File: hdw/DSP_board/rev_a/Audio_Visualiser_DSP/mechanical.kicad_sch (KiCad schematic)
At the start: 0 parts

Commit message: more schematic progress
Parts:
- added H? (x4): MountingHole, MountingHole:MountingHole_3mm, symbol Mechanical:MountingHole
- added MK? (x4): Screw, symbol Custom Library:Screw
- added MK? (x4): Standoff, symbol Custom Library:Standoff

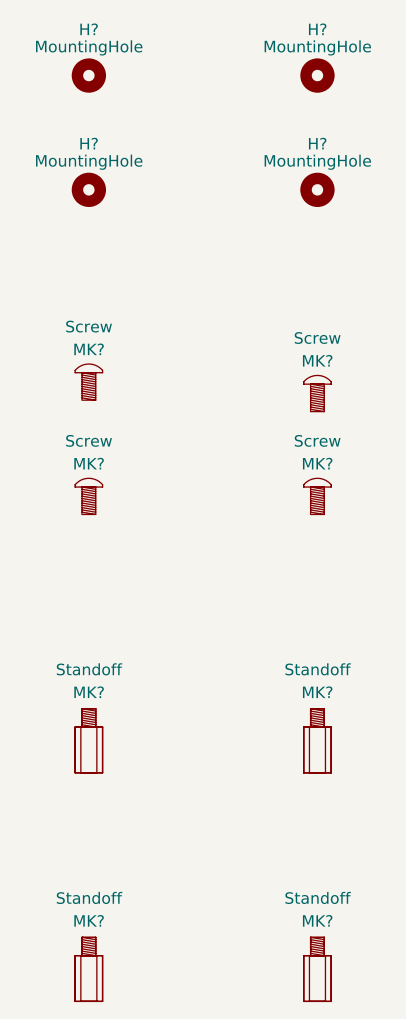
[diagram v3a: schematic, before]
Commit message: Added some spice models
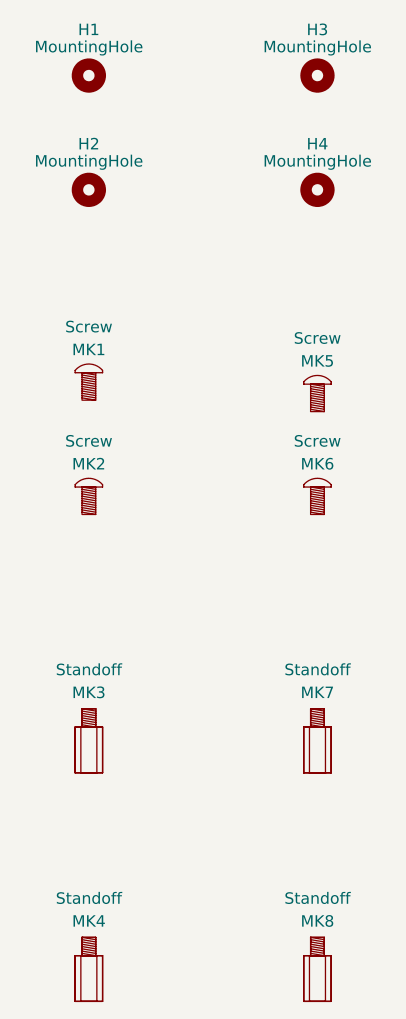
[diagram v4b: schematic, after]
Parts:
- gave numbers to parts that had none: 12
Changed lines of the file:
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@@
 		(in_pos_files yes)
 		(dnp no)
-		(property "Reference" "MK?"
+		(property "Reference" "MK6"
 			(at 139.7 99.06 0)
 			(show_name no)
@@
 			(project "Audio_Visualiser_DSP"
 				(path "/97a4dfb8-0e16-46f1-9709-8d2007dd0cd3/0b5ba344-fa98-45fc-87ea-1c2bd832dac8"
-					(reference "MK?")
+					(reference "MK6")
 					(unit 1)
 				)
@@
 		(in_pos_files yes)
 		(dnp no)
-		(property "Reference" "H?"
+		(property "Reference" "H3"
 			(at 139.7 50.8 0)
 			(show_name no)
@@
 			(project "Audio_Visualiser_DSP"
 				(path "/97a4dfb8-0e16-46f1-9709-8d2007dd0cd3/0b5ba344-fa98-45fc-87ea-1c2bd832dac8"
-					(reference "H?")
+					(reference "H3")
 					(unit 1)
 				)
@@
 		(in_pos_files yes)
 		(dnp no)
-		(property "Reference" "MK?"
+		(property "Reference" "MK7"
 			(at 139.7 124.46 0)
 			(show_name no)
@@
 			(project "Audio_Visualiser_DSP"
 				(path "/97a4dfb8-0e16-46f1-9709-8d2007dd0cd3/0b5ba344-fa98-45fc-87ea-1c2bd832dac8"
-					(reference "MK?")
+					(reference "MK7")
 					(unit 1)
 				)
@@
 		(in_pos_files yes)
 		(dnp no)
-		(property "Reference" "MK?"
+		(property "Reference" "MK3"
 			(at 114.3 124.46 0)
 			(show_name no)
@@
 			(project "Audio_Visualiser_DSP"
 				(path "/97a4dfb8-0e16-46f1-9709-8d2007dd0cd3/0b5ba344-fa98-45fc-87ea-1c2bd832dac8"
-					(reference "MK?")
+					(reference "MK3")
 					(unit 1)
 				)
@@
 		(in_pos_files yes)
 		(dnp no)
-		(property "Reference" "MK?"
+		(property "Reference" "MK1"
 			(at 114.3 86.36 0)
 			(show_name no)
@@
 			(project "Audio_Visualiser_DSP"
 				(path "/97a4dfb8-0e16-46f1-9709-8d2007dd0cd3/0b5ba344-fa98-45fc-87ea-1c2bd832dac8"
-					(reference "MK?")
+					(reference "MK1")
 					(unit 1)
 				)
@@
 		(in_pos_files yes)
 		(dnp no)
-		(property "Reference" "MK?"
+		(property "Reference" "MK2"
 			(at 114.3 99.06 0)
 			(show_name no)
@@
 			(project "Audio_Visualiser_DSP"
 				(path "/97a4dfb8-0e16-46f1-9709-8d2007dd0cd3/0b5ba344-fa98-45fc-87ea-1c2bd832dac8"
-					(reference "MK?")
+					(reference "MK2")
 					(unit 1)
 				)
@@
 		(in_pos_files yes)
 		(dnp no)
-		(property "Reference" "MK?"
+		(property "Reference" "MK8"
 			(at 139.7 149.86 0)
 			(show_name no)
@@
 			(project "Audio_Visualiser_DSP"
 				(path "/97a4dfb8-0e16-46f1-9709-8d2007dd0cd3/0b5ba344-fa98-45fc-87ea-1c2bd832dac8"
-					(reference "MK?")
+					(reference "MK8")
 					(unit 1)
 				)
@@
 		(in_pos_files yes)
 		(dnp no)
-		(property "Reference" "H?"
+		(property "Reference" "H2"
 			(at 114.3 63.5 0)
 			(show_name no)
@@
 			(project "Audio_Visualiser_DSP"
 				(path "/97a4dfb8-0e16-46f1-9709-8d2007dd0cd3/0b5ba344-fa98-45fc-87ea-1c2bd832dac8"
-					(reference "H?")
+					(reference "H2")
 					(unit 1)
 				)
@@
 		(in_pos_files yes)
 		(dnp no)
-		(property "Reference" "MK?"
+		(property "Reference" "MK5"
 			(at 139.7 87.63 0)
 			(show_name no)
@@
 			(project "Audio_Visualiser_DSP"
 				(path "/97a4dfb8-0e16-46f1-9709-8d2007dd0cd3/0b5ba344-fa98-45fc-87ea-1c2bd832dac8"
-					(reference "MK?")
+					(reference "MK5")
 					(unit 1)
 				)
@@
 		(in_pos_files yes)
 		(dnp no)
-		(property "Reference" "H?"
+		(property "Reference" "H4"
 			(at 139.7 63.5 0)
 			(show_name no)
@@
 			(project "Audio_Visualiser_DSP"
 				(path "/97a4dfb8-0e16-46f1-9709-8d2007dd0cd3/0b5ba344-fa98-45fc-87ea-1c2bd832dac8"
-					(reference "H?")
+					(reference "H4")
 					(unit 1)
 				)
@@
 		(in_pos_files yes)
 		(dnp no)
-		(property "Reference" "H?"
+		(property "Reference" "H1"
 			(at 114.3 50.8 0)
 			(show_name no)
@@
 			(project "Audio_Visualiser_DSP"
 				(path "/97a4dfb8-0e16-46f1-9709-8d2007dd0cd3/0b5ba344-fa98-45fc-87ea-1c2bd832dac8"
-					(reference "H?")
+					(reference "H1")
 					(unit 1)
 				)
@@
 		(in_pos_files yes)
 		(dnp no)
-		(property "Reference" "MK?"
+		(property "Reference" "MK4"
 			(at 114.3 149.86 0)
 			(show_name no)
@@
 			(project "Audio_Visualiser_DSP"
 				(path "/97a4dfb8-0e16-46f1-9709-8d2007dd0cd3/0b5ba344-fa98-45fc-87ea-1c2bd832dac8"
-					(reference "MK?")
-					(unit 1)
-				)
+					(reference "MK4")
+					(unit 1)
+				)

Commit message: Annotated schematic
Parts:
- renumbered H1 to H2001, H2 to H2002, H3 to H2003, H4 to H2004, MK1 to MK2001, MK2 to MK2002, MK3 to MK2003, MK4 to MK2004, MK5 to MK2005, MK6 to MK2006, MK7 to MK2007, MK8 to MK2008
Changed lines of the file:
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@@
 		(in_pos_files yes)
 		(dnp no)
-		(property "Reference" "MK6"
+		(property "Reference" "MK2006"
 			(at 139.7 99.06 0)
 			(show_name no)
@@
 			(project "Audio_Visualiser_DSP"
 				(path "/97a4dfb8-0e16-46f1-9709-8d2007dd0cd3/0b5ba344-fa98-45fc-87ea-1c2bd832dac8"
-					(reference "MK6")
+					(reference "MK2006")
 					(unit 1)
 				)
@@
 		(in_pos_files yes)
 		(dnp no)
-		(property "Reference" "H3"
+		(property "Reference" "H2003"
 			(at 139.7 50.8 0)
 			(show_name no)
@@
 			(project "Audio_Visualiser_DSP"
 				(path "/97a4dfb8-0e16-46f1-9709-8d2007dd0cd3/0b5ba344-fa98-45fc-87ea-1c2bd832dac8"
-					(reference "H3")
+					(reference "H2003")
 					(unit 1)
 				)
@@
 		(in_pos_files yes)
 		(dnp no)
-		(property "Reference" "MK7"
+		(property "Reference" "MK2007"
 			(at 139.7 124.46 0)
 			(show_name no)
@@
 			(project "Audio_Visualiser_DSP"
 				(path "/97a4dfb8-0e16-46f1-9709-8d2007dd0cd3/0b5ba344-fa98-45fc-87ea-1c2bd832dac8"
-					(reference "MK7")
+					(reference "MK2007")
 					(unit 1)
 				)
@@
 		(in_pos_files yes)
 		(dnp no)
-		(property "Reference" "MK3"
+		(property "Reference" "MK2003"
 			(at 114.3 124.46 0)
 			(show_name no)
@@
 			(project "Audio_Visualiser_DSP"
 				(path "/97a4dfb8-0e16-46f1-9709-8d2007dd0cd3/0b5ba344-fa98-45fc-87ea-1c2bd832dac8"
-					(reference "MK3")
+					(reference "MK2003")
 					(unit 1)
 				)
@@
 		(in_pos_files yes)
 		(dnp no)
-		(property "Reference" "MK1"
+		(property "Reference" "MK2001"
 			(at 114.3 86.36 0)
 			(show_name no)
@@
 			(project "Audio_Visualiser_DSP"
 				(path "/97a4dfb8-0e16-46f1-9709-8d2007dd0cd3/0b5ba344-fa98-45fc-87ea-1c2bd832dac8"
-					(reference "MK1")
+					(reference "MK2001")
 					(unit 1)
 				)
@@
 		(in_pos_files yes)
 		(dnp no)
-		(property "Reference" "MK2"
+		(property "Reference" "MK2002"
 			(at 114.3 99.06 0)
 			(show_name no)
@@
 			(project "Audio_Visualiser_DSP"
 				(path "/97a4dfb8-0e16-46f1-9709-8d2007dd0cd3/0b5ba344-fa98-45fc-87ea-1c2bd832dac8"
-					(reference "MK2")
+					(reference "MK2002")
 					(unit 1)
 				)
@@
 		(in_pos_files yes)
 		(dnp no)
-		(property "Reference" "MK8"
+		(property "Reference" "MK2008"
 			(at 139.7 149.86 0)
 			(show_name no)
@@
 			(project "Audio_Visualiser_DSP"
 				(path "/97a4dfb8-0e16-46f1-9709-8d2007dd0cd3/0b5ba344-fa98-45fc-87ea-1c2bd832dac8"
-					(reference "MK8")
+					(reference "MK2008")
 					(unit 1)
 				)
@@
 		(in_pos_files yes)
 		(dnp no)
-		(property "Reference" "H2"
+		(property "Reference" "H2002"
 			(at 114.3 63.5 0)
 			(show_name no)
@@
 			(project "Audio_Visualiser_DSP"
 				(path "/97a4dfb8-0e16-46f1-9709-8d2007dd0cd3/0b5ba344-fa98-45fc-87ea-1c2bd832dac8"
-					(reference "H2")
+					(reference "H2002")
 					(unit 1)
 				)
@@
 		(in_pos_files yes)
 		(dnp no)
-		(property "Reference" "MK5"
+		(property "Reference" "MK2005"
 			(at 139.7 87.63 0)
 			(show_name no)
@@
 			(project "Audio_Visualiser_DSP"
 				(path "/97a4dfb8-0e16-46f1-9709-8d2007dd0cd3/0b5ba344-fa98-45fc-87ea-1c2bd832dac8"
-					(reference "MK5")
+					(reference "MK2005")
 					(unit 1)
 				)
@@
 		(in_pos_files yes)
 		(dnp no)
-		(property "Reference" "H4"
+		(property "Reference" "H2004"
 			(at 139.7 63.5 0)
 			(show_name no)
@@
 			(project "Audio_Visualiser_DSP"
 				(path "/97a4dfb8-0e16-46f1-9709-8d2007dd0cd3/0b5ba344-fa98-45fc-87ea-1c2bd832dac8"
-					(reference "H4")
+					(reference "H2004")
 					(unit 1)
 				)
@@
 		(in_pos_files yes)
 		(dnp no)
-		(property "Reference" "H1"
+		(property "Reference" "H2001"
 			(at 114.3 50.8 0)
 			(show_name no)
@@
 			(project "Audio_Visualiser_DSP"
 				(path "/97a4dfb8-0e16-46f1-9709-8d2007dd0cd3/0b5ba344-fa98-45fc-87ea-1c2bd832dac8"
-					(reference "H1")
+					(reference "H2001")
 					(unit 1)
 				)
@@
 		(in_pos_files yes)
 		(dnp no)
-		(property "Reference" "MK4"
+		(property "Reference" "MK2004"
 			(at 114.3 149.86 0)
 			(show_name no)
@@
 			(project "Audio_Visualiser_DSP"
 				(path "/97a4dfb8-0e16-46f1-9709-8d2007dd0cd3/0b5ba344-fa98-45fc-87ea-1c2bd832dac8"
-					(reference "MK4")
-					(unit 1)
-				)
+					(reference "MK2004")
+					(unit 1)
+				)

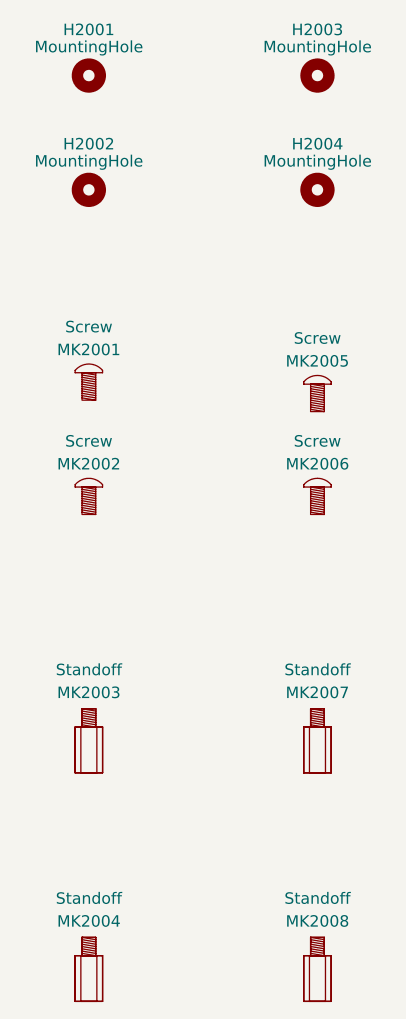
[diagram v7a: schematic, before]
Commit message: Added a bunch of stuff to the schematic
Moved to adafruit I2C rotary encoder module. Added signal test points. Added some design schematic notes. Added LEd output connector ESD diodes. Consolidated on a single schottky diode. Connected most signals to MCU
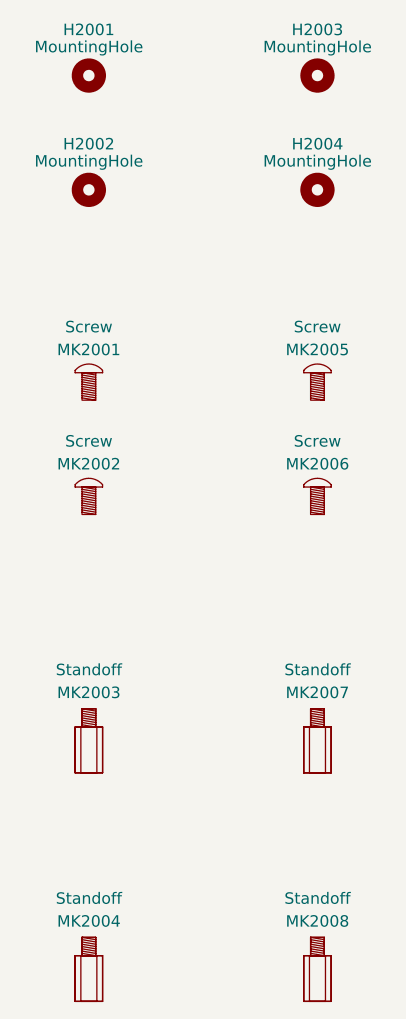
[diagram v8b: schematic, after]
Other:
- moved on the sheet: MK2005
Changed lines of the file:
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@@
 	(symbol
 		(lib_id "Custom Library:Screw")
-		(at 139.7 90.17 0)
+		(at 139.7 88.9 0)
 		(unit 1)
 		(body_style 1)
@@
 		(dnp no)
 		(property "Reference" "MK2005"
-			(at 139.7 87.63 0)
+			(at 139.7 86.36 0)
 			(show_name no)
 			(do_not_autoplace no)
@@
 		)
 		(property "Value" "Screw"
-			(at 139.7 85.09 0)
+			(at 139.7 83.82 0)
 			(show_name no)
 			(do_not_autoplace no)
@@
 		)
 		(property "Footprint" ""
-			(at 139.7 83.82 0)
+			(at 139.7 82.55 0)
 			(hide yes)
 			(show_name no)
@@
 		)
 		(property "Datasheet" ""
-			(at 139.7 83.82 0)
+			(at 139.7 82.55 0)
 			(hide yes)
 			(show_name no)
@@
 		)
 		(property "Description" ""
-			(at 139.7 90.17 0)
+			(at 139.7 88.9 0)
 			(hide yes)
 			(show_name no)
@@
 		)
 		(property "Sim.Type" ""
-			(at 139.7 90.17 0)
+			(at 139.7 88.9 0)
 			(hide yes)
 			(show_name no)
